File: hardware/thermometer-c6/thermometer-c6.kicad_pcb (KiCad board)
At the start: 2 copper layers, 48 x 35 mm, 101 parts, among them J1 JST-PH-2 BAT, J2 MEAS_HDR, J3 USB-C, J4 EPD FPC24 0.5mm, J5 DEBUG, Q1 AO3401A, Q2 AO3401A, Q3 Si1308EDL, Q4 AO3401A, Q5 2N7002, Q6 AO3401A, SW1 RESET, SW2 BOOT, U1 ESP32-C6-MINI-1-N4, U2 RT9080-33GJ5, U3 USBLC6-2SC6, U4 MCP73831-2, U5 BMP581, U6 BMP585, Y1 32.768kHz FC-135

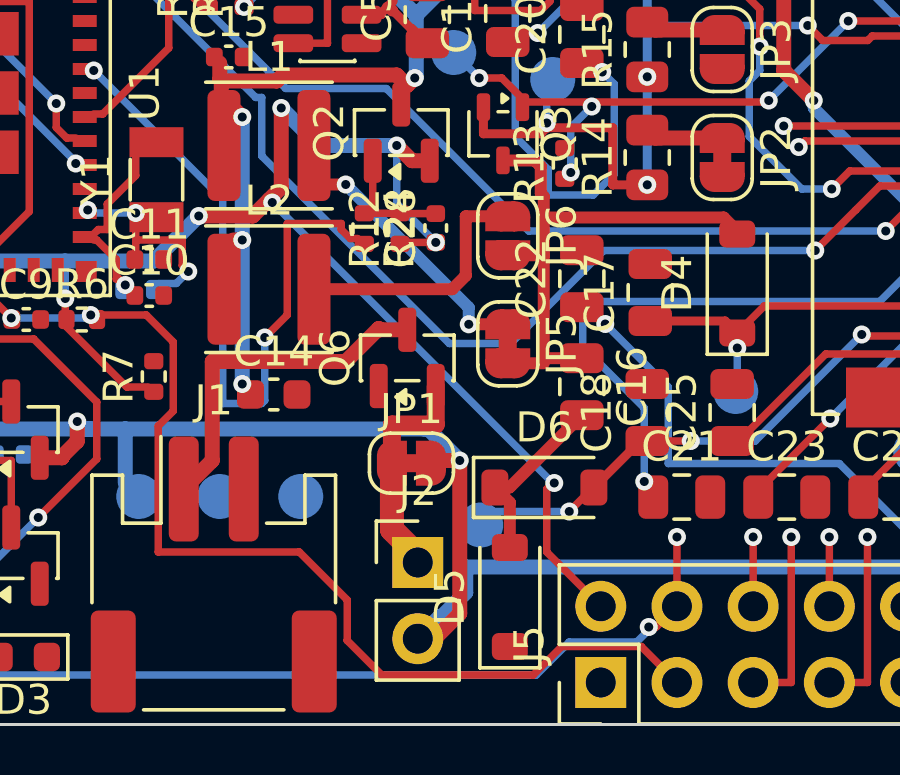
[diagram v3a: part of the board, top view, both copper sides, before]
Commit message: Move TP7 out of the south corridor's pinch band
Its 2.1mm HV B.Cu wall pinched x28.7..31.1 to a 0.30mm slot at y~27.0.
The pad now sits between C16 and D6 on the bottom face, beside the
copper it senses (D6.2/C18.1), clear of the corridor's east-running
band and of the pocket descent slots. Straggler list unchanged (15).

Co-Authored-By: Claude Fable 5 <noreply@anthropic.com>
Claude-Session: https://claude.ai/code/session_01SwxdfLoUnFYH7rYYztLkHV
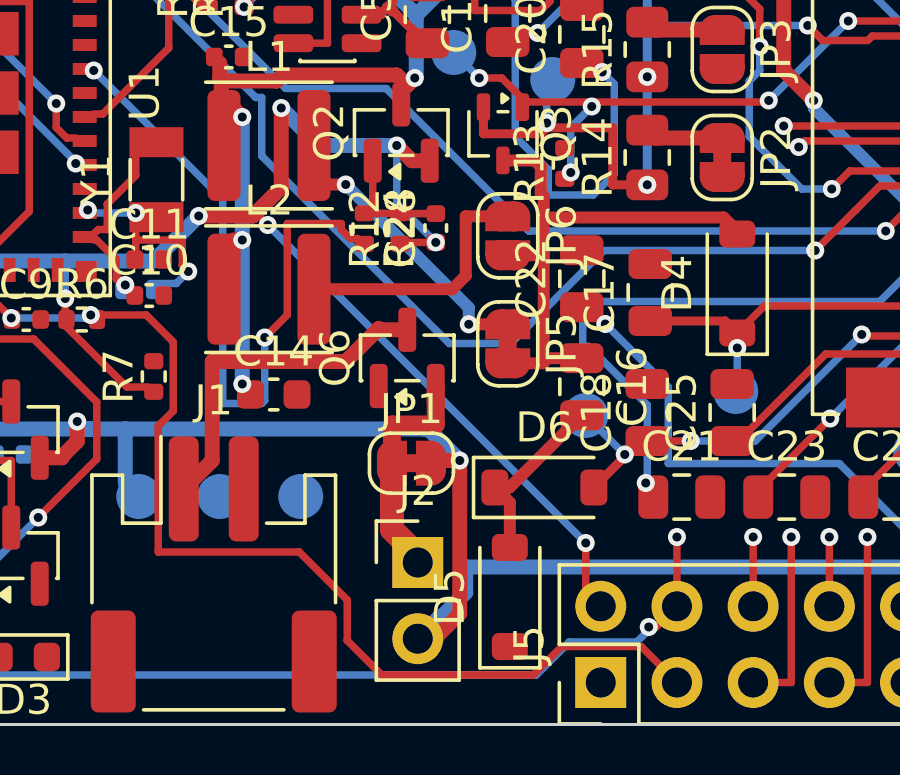
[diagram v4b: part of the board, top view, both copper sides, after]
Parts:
- TP7: renamed from TP9; value RESE -> PREVGL
- TP9: renamed from TP7; value PREVGL -> RESE
- moved TP9 15.0 mm to (132.3, 113.5)
- moved TP7 11.3 mm to (133.4, 124.7)
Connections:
- TP7 pad 1: EPD_RESE -> EPD_PREVGL
- TP9 pad 1: EPD_PREVGL -> EPD_RESE
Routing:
- net EPD_PREVGL: track 17.8 -> 15.4 mm
- net +3V3: track 90.6 -> 90.0 mm
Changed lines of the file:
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@@
 	(footprint "TestPoint:TestPoint_Pad_D1.5mm"
 		(layer "B.Cu")
-		(at 129.9 128.35)
+		(at 132.3 113.5)
 		(descr "SMD pad as test Point, diameter 1.5mm")
 		(tags "test point SMD pad")
-		(property "Reference" "TP7"
+		(property "Reference" "TP9"
 			(at 0 1.648 180)
 			(layer "B.SilkS")
@@
 			)
 		)
-		(property "Value" "PREVGL"
+		(property "Value" "RESE"
 			(at 0 -1.75 180)
 			(layer "B.Fab")
@@
 			(size 1.5 1.5)
 			(layers "B.Cu" "B.Mask")
-			(net "EPD_PREVGL")
+			(net "EPD_RESE")
 		)
 		(embedded_fonts no)
@@
 	(footprint "TestPoint:TestPoint_Pad_D1.5mm"
 		(layer "B.Cu")
-		(at 132.3 113.5)
+		(at 133.4 124.7)
 		(descr "SMD pad as test Point, diameter 1.5mm")
 		(tags "test point SMD pad")
-		(property "Reference" "TP9"
+		(property "Reference" "TP7"
 			(at 0 1.648 180)
 			(layer "B.SilkS")
@@
 			)
 		)
-		(property "Value" "RESE"
+		(property "Value" "PREVGL"
 			(at 0 -1.75 180)
 			(layer "B.Fab")
@@
 			(size 1.5 1.5)
 			(layers "B.Cu" "B.Mask")
-			(net "EPD_RESE")
+			(net "EPD_PREVGL")
 		)
 		(embedded_fonts no)
@@
 	(segment
 		(start 122.3 118.05)
-		(end 122.85 117.5)
+		(end 122.4 117.95)
 		(width 0.5)
 		(layer "F.Cu")
@@
 	)
 	(segment
+		(start 122.4 117.95)
+		(end 123.25 117.1)
+		(width 0.5)
+		(layer "F.Cu")
+		(net "+3V3")
+	)
+	(segment
 		(start 122.6 114.1)
 		(end 122.6 116.05)
@@
 	)
 	(segment
-		(start 122.85 117.5)
-		(end 123.25 117.1)
-		(width 0.5)
+		(start 122.8 118.35)
+		(end 122.4 117.95)
+		(width 0.25)
 		(layer "F.Cu")
 		(net "+3V3")
 	)
 	(segment
-		(start 122.95 117.6)
-		(end 122.85 117.5)
+		(start 122.800001 118.35)
+		(end 122.8 118.35)
 		(width 0.25)
-		(layer "F.Cu")
+		(layer "B.Cu")
 		(net "+3V3")
 	)
@@
 	)
 	(segment
-		(start 130.35 127.9)
-		(end 132.85 127.9)
-		(width 0.25)
-		(layer "B.Cu")
-		(net "EPD_PREVGL")
-	)
-	(segment
 		(start 130.37 127.1)
 		(end 130.87 127.6)
@@
 	)
 	(segment
-		(start 132.1 127.15)
-		(end 132.3 126.95)
-		(width 0.25)
-		(layer "F.Cu")
-		(net "+3V3")
-	)
-	(segment
-		(start 132.1 129.25)
-		(end 132.1 127.15)
-		(width 0.25)
-		(layer "F.Cu")
-		(net "+3V3")
-	)
-	(segment
 		(start 132.15 116.5)
 		(end 131.05 115.4)
@@
 	)
 	(segment
-		(start 132.3 126.95)
-		(end 122.95 117.6)
-		(width 0.25)
-		(layer "B.Cu")
-		(net "+3V3")
-	)
-	(segment
-		(start 132.3 126.95)
-		(end 132.35 126.95)
-		(width 0.25)
-		(layer "F.Cu")
-		(net "+3V3")
-	)
-	(segment
-		(start 132.35 126.95)
-		(end 132.3 126.95)
-		(width 0.25)
-		(layer "B.Cu")
-		(net "+3V3")
-	)
-	(segment
 		(start 132.4 105.7)
 		(end 133.4 105.7)
@@
 	)
 	(segment
-		(start 132.85 127.9)
-		(end 133.65 127.1)
-		(width 0.25)
-		(layer "F.Cu")
-		(net "EPD_PREVGL")
-	)
-	(segment
 		(start 132.85 132.25)
 		(end 135.1 132.25)
@@
 	)
 	(segment
+		(start 133.4 128.949999)
+		(end 122.800001 118.35)
+		(width 0.25)
+		(layer "B.Cu")
+		(net "+3V3")
+	)
+	(segment
 		(start 133.4 130.55)
-		(end 132.1 129.25)
+		(end 133.4 128.949999)
 		(width 0.25)
 		(layer "F.Cu")
@@
 	)
 	(segment
+		(start 133.5 122.4)
+		(end 133.3 122.4)
+		(width 0.25)
+		(layer "B.Cu")
+		(net "Net-(J4-Pin_18)")
+	)
+	(segment
 		(start 133.6 114.25)
 		(end 139.45 114.25)
@@
 	)
 	(segment
+		(start 133.85 125.15)
+		(end 134.7 126)
+		(width 0.25)
+		(layer "B.Cu")
+		(net "EPD_PREVGL")
+	)
+	(segment
 		(start 133.949999 113.25)
 		(end 134.349999 113.65)
@@
 	)
 	(segment
+		(start 134.7 126)
+		(end 134.75 126)
+		(width 0.25)
+		(layer "F.Cu")
+		(net "EPD_PREVGL")
+	)
+	(segment
 		(start 135.1 132.25)
 		(end 135.5 131.85)
@@
 	)
 	(segment
-		(start 135.35 124.45)
-		(end 133.3 122.4)
-		(width 0.25)
-		(layer "B.Cu")
-		(net "Net-(J4-Pin_18)")
-	)
-	(segment
-		(start 135.35 126.9)
-		(end 135.35 124.45)
+		(start 135.4 126.95)
+		(end 135.45 126.9)
 		(width 0.25)
 		(layer "B.Cu")
@@
 	)
 	(segment
+		(start 135.45 124.35)
+		(end 133.5 122.4)
+		(width 0.25)
+		(layer "B.Cu")
+		(net "Net-(J4-Pin_18)")
+	)
+	(segment
+		(start 135.45 126.9)
+		(end 135.45 124.35)
+		(width 0.25)
+		(layer "B.Cu")
+		(net "Net-(J4-Pin_18)")
+	)
+	(segment
 		(start 135.5 131.75)
 		(end 135.75 131.75)
@@
 	)
 	(via
-		(at 122.95 117.6)
+		(at 122.8 118.35)
 		(size 0.6)
 		(drill 0.3)
@@
 	)
 	(via
-		(at 132.35 126.95)
-		(size 0.6)
-		(drill 0.3)
-		(layers "F.Cu" "B.Cu")
-		(net "+3V3")
-	)
-	(via
 		(at 132.55 109.35)
 		(size 0.6)
@@
 	)
 	(via
-		(at 132.85 127.9)
+		(at 132.9 116.6)
 		(size 0.6)
 		(drill 0.3)
 		(layers "F.Cu" "B.Cu")
-		(net "EPD_PREVGL")
+		(net "EPD_GDR")
 	)
 	(via
-		(at 132.9 116.6)
+		(at 133.4 128.949999)
 		(size 0.6)
 		(drill 0.3)
 		(layers "F.Cu" "B.Cu")
-		(net "EPD_GDR")
+		(net "+3V3")
 	)
 	(via
@@
 	)
 	(via
-		(at 135.35 126.9)
+		(at 134.7 126)
+		(size 0.6)
+		(drill 0.3)
+		(layers "F.Cu" "B.Cu")
+		(net "EPD_PREVGL")
+	)
+	(via
+		(at 135.4 126.95)
 		(size 0.6)
 		(drill 0.3)

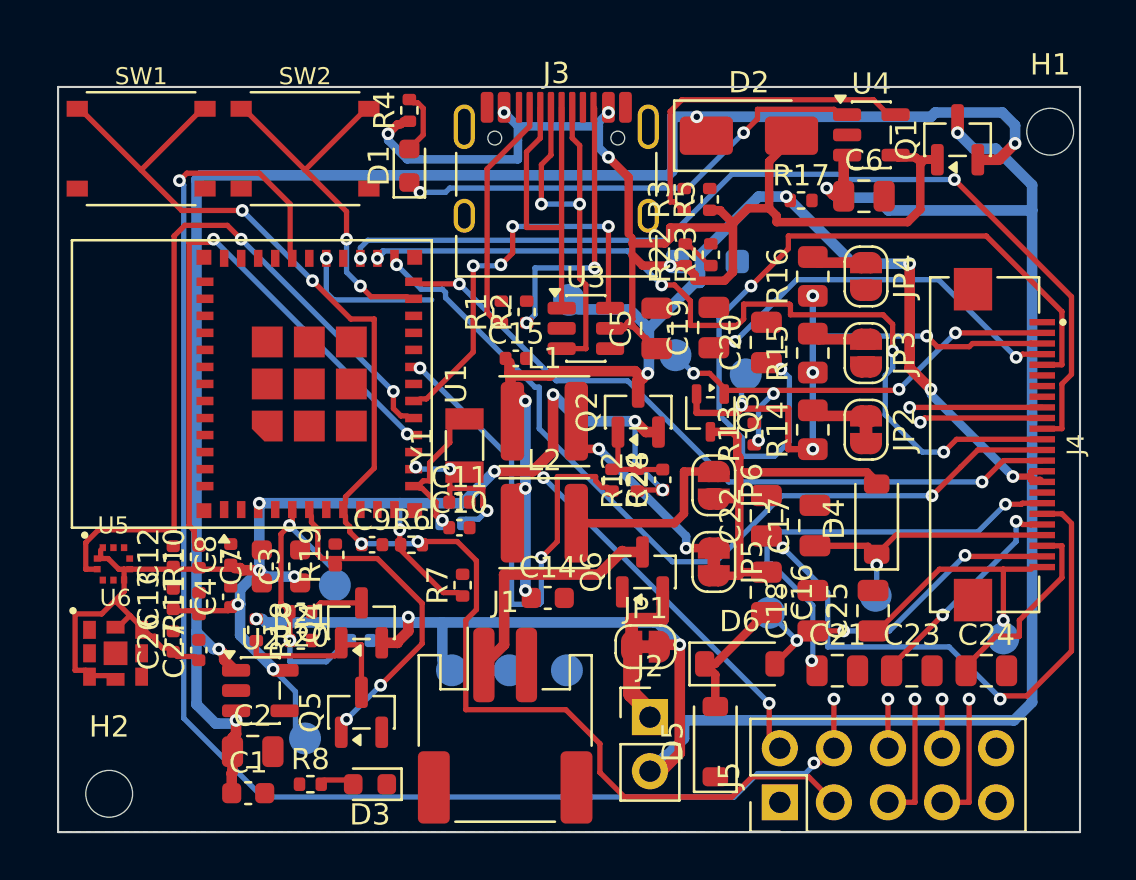
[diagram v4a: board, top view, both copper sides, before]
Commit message: Author the U1-to-J5 debug lanes end to end; move TP9 off the RESE seam
DBG_TX/RX/IO8 now cross under the module in the y12.75..13.65 band
(north of EPD_VCC's spine via, south of the east pad row's via strip),
dive past the +3V3 elbow, descend at x30.2/30.65/31.75 and cross the
pocket floor to their J5 fan-in vias. VBUS_SENSE/DBG_IO5 get their
south-row escape vias; XTAL_32K_N's U1.13 hop is authored so USB_D+
cannot steal its seam; J5.2's +3V3 feed runs along the south edge
instead of letting the router wall the pocket floor; TP9 kisses the
RESE sense column, freeing the only B.Cu seam east of the booster.

15 -> 19 stragglers, but the remaining set is now concentrated where
placement work is still pending: the U1 NE gate (SCK/CS/DC/RST/D+),
BOOT/R7, the sensor corner, and the south corridor pair. Known issue:
EPD_MOSI temporarily bypasses its authored staircase via (dangling)
until the gate cluster is reworked.

Co-Authored-By: Claude Fable 5 <noreply@anthropic.com>
Claude-Session: https://claude.ai/code/session_01SwxdfLoUnFYH7rYYztLkHV
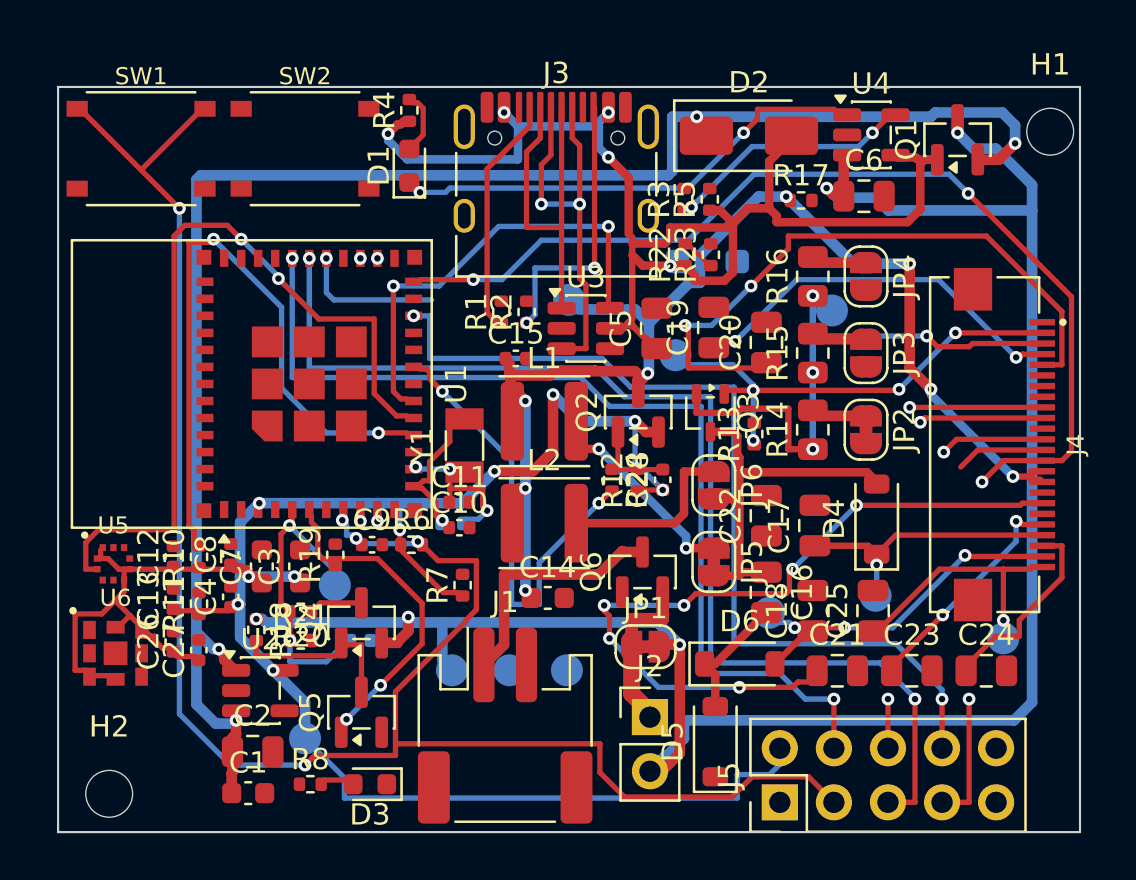
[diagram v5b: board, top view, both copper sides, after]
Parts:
- TP7: renamed from TP9; value RESE -> PREVGL
- TP9: renamed from TP7; value PREVGL -> RESE
- moved TP9 14.5 mm to (136.3, 110.5)
- moved TP7 11.3 mm to (133.4, 124.7)
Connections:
- TP7 pad 1: EPD_RESE -> EPD_PREVGL
- TP9 pad 1: EPD_PREVGL -> EPD_RESE
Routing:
- net DBG_RX: track 6.12 -> 53.5 mm, vias 1 -> 2
- net EPD_DC: track 44.5 -> 0.00 mm, vias 2 -> 1
- net DBG_IO8: track 2.31 -> 43.1 mm, vias 1 -> 2
- net EPD_CS: track 40.8 -> 4.87 mm, vias 4 -> 2
- net EPD_SCK: track 39.6 -> 4.16 mm, vias 2 -> 0
- net Net-(J4-Pin_19): track 26.3 -> 0.00 mm, vias 2 -> 0
- net DBG_TX: track 68.9 -> 47.0 mm, vias 3 -> 2
- net EN: track 65.2 -> 86.3 mm, vias 4 -> 5
- net BOOT: track 16.4 -> 0.00 mm, vias 2 -> 0
- net Net-(J4-Pin_18): track 20.0 -> 34.7 mm, vias 2 -> 6
- net EPD_MOSI: track 33.5 -> 47.1 mm, vias 2 -> 3
- net +3V3: track 90.0 -> 100.2 mm, vias 12 -> 10
- net Net-(J4-Pin_5): track 35.6 -> 29.4 mm
- net Net-(U4-PROG): track 15.3 -> 11.0 mm, vias 0 -> 2
- net EPD_PWR_EN: track 23.2 -> 20.8 mm
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
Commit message: Move R7 beside SW2, into BOOT's crossing zone
At (19.0, 23.4) the BOOT pull-up halved the x17.1..19.15 F.Cu column --
the south corridor's only crossing of the VBAT wall -- and sat 13mm from
U1.23 across the crystal block, leaving BOOT unroutable to R7.2 and,
with the debug lanes in place, to SW2. All three BOOT stragglers clear;
the column is now four lanes wide for EN and the VBUS_SENSE/DBG_IO5
pair. 19 -> 16.

Co-Authored-By: Claude Fable 5 <noreply@anthropic.com>
Claude-Session: https://claude.ai/code/session_01SwxdfLoUnFYH7rYYztLkHV
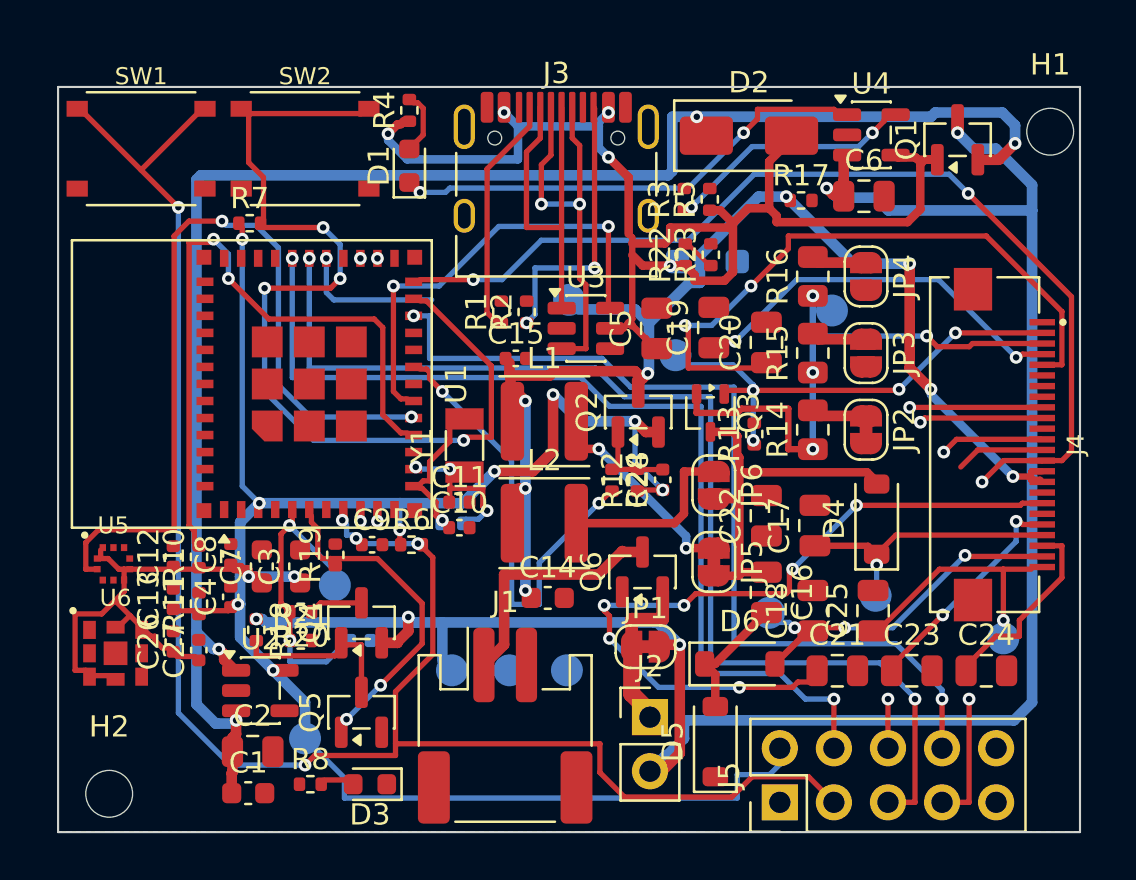
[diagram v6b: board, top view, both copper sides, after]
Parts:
- R18: renamed from R20; value 100k 1% -> 100k
- R19: renamed from R4; value 1k -> 100k
- R21: renamed from R8; value 1k -> 100k 1%
- R4: renamed from R6; value 10k -> 1k
- R7: renamed from R18; value 100k -> 10k
- R8: renamed from R19; value 100k -> 1k
- moved R19 21.2 mm to (113.0, 122.0)
- moved R4 20.4 mm to (116.5, 101.1), turned to 90 degrees
- moved R7 19.1 mm to (109.0, 106.4), turned to 0 degrees
- moved R8 10.8 mm to (111.8, 132.8), turned to 0 degrees
- moved R21 6.76 mm to (111.4, 126.0)
- moved R6 3.06 mm to (116.6, 121.5), turned to 0 degrees
- moved R18 2.26 mm to (109.3, 125.5), turned to -90 degrees
- moved R20 1.35 mm to (111.4, 124.7), turned to 180 degrees
- renumbered R21 to R20, R7 to R6
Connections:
- R18 pad 1: Net-(Q4-D) -> VBAT
- R18 pad 2: VBAT_ADC -> Net-(Q4-G)
- R19 pad 1: VBUS -> VDIV_EN
- R19 pad 2: Net-(D1-A) -> GND
- R20 pad 1: VBAT_ADC -> Net-(Q4-D)
- R20 pad 2: GND -> VBAT_ADC
- R21 pad 1: LED_STATUS -> VBAT_ADC
- R21 pad 2: Net-(D3-A) -> GND
- R4 pad 1: +3V3 -> VBUS
- R4 pad 2: EN -> Net-(D1-A)
- R6 pad 2: BOOT -> EN
- R7 pad 1: VBAT -> +3V3
- R7 pad 2: Net-(Q4-G) -> BOOT
- R8 pad 1: VDIV_EN -> LED_STATUS
- R8 pad 2: GND -> Net-(D3-A)
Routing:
- net BOOT: track 0.00 -> 44.7 mm, vias 0 -> 4
- net +3V3: track 100.2 -> 109.5 mm, vias 10 -> 11
- net EN: track 86.3 -> 83.4 mm
- net SCL: track 36.9 -> 38.9 mm
- net SDA: track 30.5 -> 31.4 mm

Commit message: Rebuild the sensor corner around south-facing I2C; author BOOT's crossing
Both sensors rotate 90 degrees so SCL/SDA leave on the south and east
faces; C12/C13/C26 vacate the x5.41 picket strip (C12 east of U5 under
the antenna keep-out margin, C13 to the SW corner, C26 below C27), and
the bus reaches U1 through the west F.Cu column instead of threading
the old double fence. SCL's U5.2 leg gets an authored F.Cu stub -- the
sensor keep-out forbids vias there and +3V3 otherwise claims the only
approach for U5.1. BOOT's U1.23-to-R7.2 crossing is authored west of
DBG_TX's via-in-pad, clear of EPD_RST's future via at (13.4, 8.05);
its B.Cu leg lands on R7.2's pad. 16 -> 13 stragglers.

Co-Authored-By: Claude Fable 5 <noreply@anthropic.com>
Claude-Session: https://claude.ai/code/session_01SwxdfLoUnFYH7rYYztLkHV
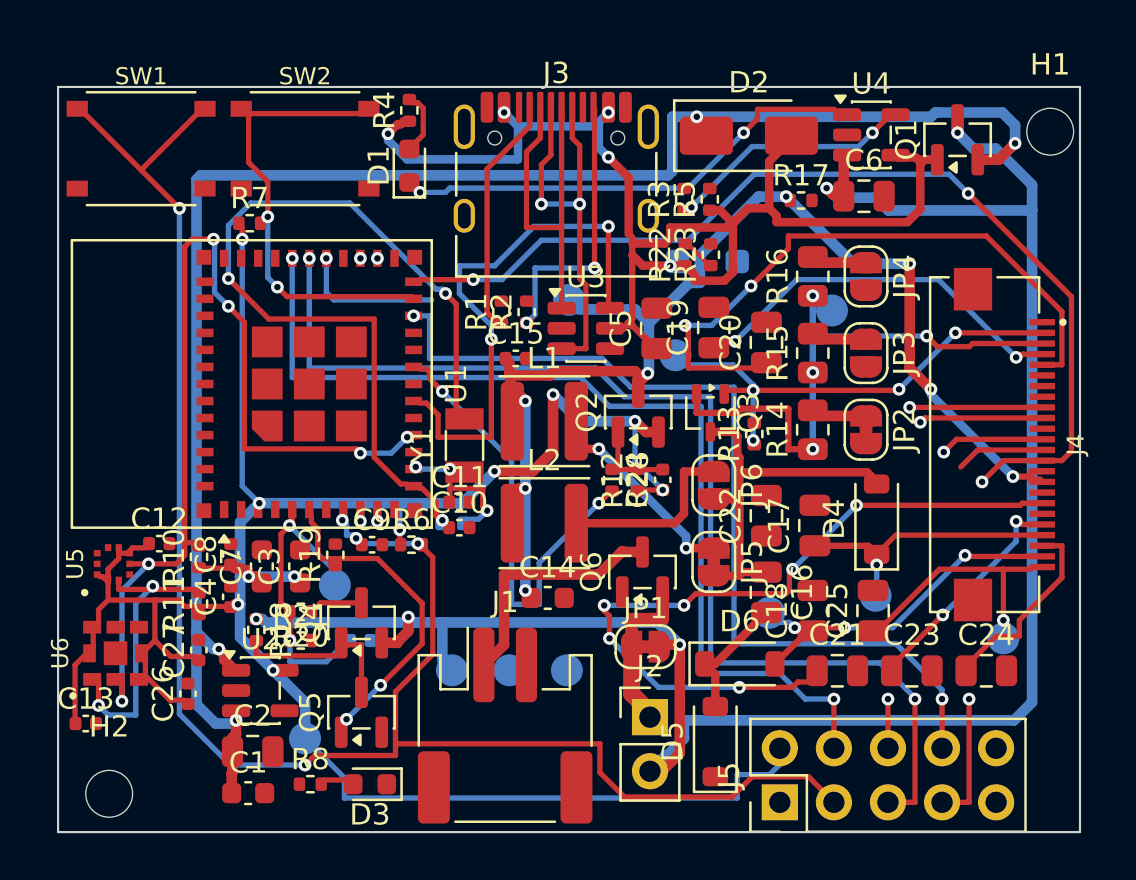
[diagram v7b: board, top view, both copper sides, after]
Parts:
- moved C13 8.86 mm to (101.3, 129.9), turned to 0 degrees
- moved C12 2.68 mm to (104.8, 121.5), turned to 0 degrees
- moved C26 2.55 mm to (106.1, 128.5)
- turned U5 to 90 degrees
- turned U6 to 90 degrees
- renumbered C13 to C12, C12 to C13
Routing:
- net XTAL_32K_P: track 5.77 -> 39.2 mm, vias 1 -> 3
- net SCL: track 38.9 -> 13.5 mm
- net BOOT: track 44.7 -> 21.1 mm, vias 4 -> 2
- net SDA: track 31.4 -> 45.4 mm, vias 2 -> 6
- net USB_D-: track 20.7 -> 24.7 mm
- net +3V3: track 109.5 -> 112.5 mm
